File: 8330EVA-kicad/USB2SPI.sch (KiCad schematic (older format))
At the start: 8 parts

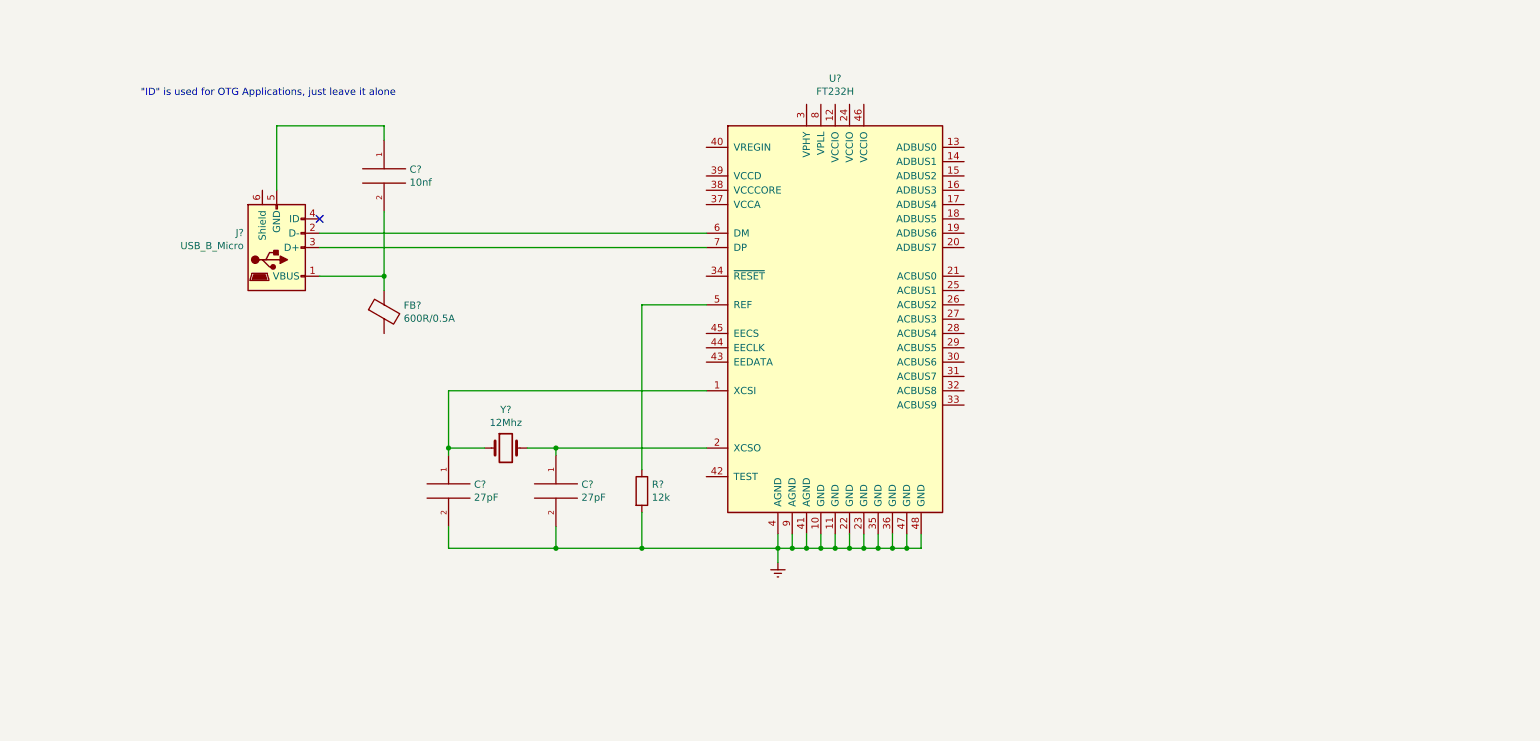
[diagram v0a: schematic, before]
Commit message: 完成FT232驱动电路原理图的绘制，并未相关的元件添加了封装
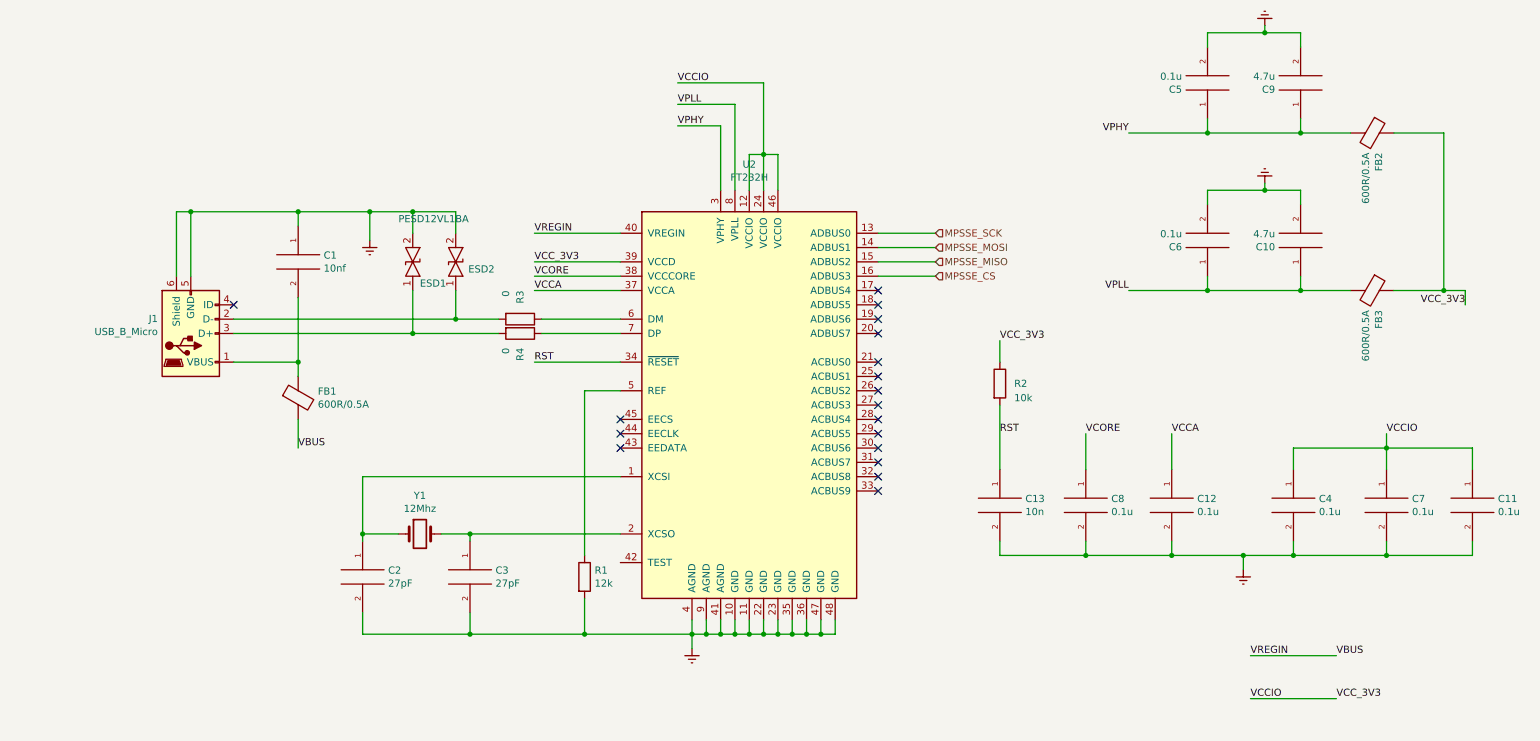
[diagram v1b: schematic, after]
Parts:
- added C10, C9: 4.7u, Capacitor_SMD:C_0603_1608Metric_Pad1.05x0.95mm_HandSolder, symbol pspice:CAP
- added C11, C12, C4, C5, C6, C7, C8: 0.1u, Capacitor_SMD:C_0603_1608Metric_Pad1.05x0.95mm_HandSolder, symbol pspice:CAP
- added C13: 10n, Capacitor_SMD:C_0603_1608Metric_Pad1.05x0.95mm_HandSolder, symbol pspice:CAP
- added ESD1, ESD2: PESD12VL1BA, Diode_SMD:D_SOD-323_HandSoldering, symbol 8330_EVA-extra:PESD12VL1BA
- added FB2, FB3: 600R/0.5A, Resistor_SMD:R_0805_2012Metric_Pad1.15x1.40mm_HandSolder, symbol Device:Ferrite_Bead
- added R2: 10k, Resistor_SMD:R_0805_2012Metric_Pad1.15x1.40mm_HandSolder, symbol Device:R
- added R3, R4: 0, Resistor_SMD:R_0805_2012Metric_Pad1.15x1.40mm_HandSolder, symbol Device:R
- C1, C2, C3: renamed from C?; footprint (none) -> Capacitor_SMD:C_0603_1608Metric_Pad1.05x0.95mm_HandSolder
- FB1: renamed from FB?; footprint (none) -> Resistor_SMD:R_0805_2012Metric_Pad1.15x1.40mm_HandSolder
- J1: renamed from J?; footprint (none) -> Connector_USB:USB_Micro-B_Wuerth_614105150721_Vertical
- R1: renamed from R?; footprint (none) -> Resistor_SMD:R_0805_2012Metric_Pad1.15x1.40mm_HandSolder
- U2: renamed from U?; footprint (none) -> Package_QFP:LQFP-48_7x7mm_P0.5mm
- Y1: renamed from Y?; footprint (none) -> Crystal:Crystal_SMD_5032-2Pin_5.0x3.2mm_HandSoldering
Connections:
- net Earth: now also C1.1, J1.5 (GND), J1.6 (Shield), C10.2, C11.2, C12.2, C13.2, C4.2, C5.2, C6.2, C7.2, C8.2, C9.2, ESD1.2, ESD2.2
- net VCCIO: now reaches U2.12 (VCCIO)
- net VCCIO: now also U2.24 (VCCIO), U2.39 (VCCD), U2.46 (VCCIO), C11.1, C4.1, C7.1, FB2.1, FB3.1, R2.1
- net MPSSE_SCK: now reaches U2.13 (ADBUS0)
- net MPSSE_MOSI: now reaches U2.14 (ADBUS1)
- net MPSSE_MISO: now reaches U2.15 (ADBUS2)
- net MPSSE_CS: now reaches U2.16 (ADBUS3)
- net VPHY: now reaches U2.3 (VPHY)
- net VPHY: now also C5.1, C9.1, FB2.2
- net RST: now reaches U2.34 (~RESET)
- net RST: now also C13.1, R2.2
- net VCCA: now reaches U2.37 (VCCA)
- net VCCA: now also C12.1
- net VCORE: now reaches U2.38 (VCCCORE)
- net VCORE: now also C8.1
- net VBUS: now reaches U2.40 (VREGIN)
- net VBUS: now also FB1.2
- net at U2.6 (DM): now also R3.1; no longer J1.2 (D-)
- net at U2.7 (DP): now also R4.1; no longer J1.3 (D+)
- net VPLL: now reaches U2.8 (VPLL)
- net VPLL: now also C10.1, C6.1, FB3.2
- new net: ESD2.1, J1.2 (D-), R3.2
- new net: ESD1.1, J1.3 (D+), R4.2
- no-connect marks 1 -> 18
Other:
- note removed: ""ID" is used for OTG Applications, just leave it alone\n"
- moved on the sheet: C1, C2, C3, FB1, J1, R1, U2, Y1

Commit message: 添加DAC部分/修改FT232供电方式（原理图）
1. 完成AD5312及REF192组成的程控信号产生部分原理图绘制
2. 修改FT232H的供电方式，添加了3.3VLDO，从之前的BUS-Power改为Self_Power
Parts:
- removed J1: USB_B_Micro, Connector_USB:USB_Micro-B_Wuerth_614105150721_Vertical, symbol Connector:USB_B_Micro
- added C?: 4.7u, symbol Device:C
- added C? (x2): 100n, symbol Device:C
- added U?: AMS1117-3.3, Package_TO_SOT_SMD:SOT-223-3_TabPin2, symbol Regulator_Linear:AMS1117-3.3
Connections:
- net VBUS: no longer U2.40 (VREGIN)
- net VCCIO: now also U2.40 (VREGIN), C?.1, U?.2 (VO)
- net USB_D-: now reaches ESD2.1, R3.2
- net USB_D+: now reaches ESD1.1, R4.2
- net Earth renamed Ground
- net Ground: now also C?.2, C?.2, C?.2, U?.1 (GND)
- new net VCC_+5V: C?.1, C?.1, U?.3 (VI)
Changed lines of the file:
@@
 	6200 5850 6100 5850
 Connection ~ 6100 5850
-$Comp
-L power:Earth #PWR0101
-U 1 1 5BEE6A05
-P 5200 5950
-F 0 "#PWR0101" H 5200 5700 50  0001 C CNN
-F 1 "Earth" H 5200 5800 50  0001 C CNN
-F 2 "" H 5200 5950 50  0001 C CNN
-F 3 "~" H 5200 5950 50  0001 C CNN
-	1    5200 5950
-	1    0    0    -1
-$EndComp
-Wire Wire Line
-	5200 5950 5200 5850
 Connection ~ 5200 5850
 $Comp
@@
 $EndComp
 $Comp
-L Connector:USB_B_Micro J1
-U 1 1 5BEF4049
-P 1700 3750
-F 0 "J1" H 1470 3647 50  0000 R CNN
-F 1 "USB_B_Micro" H 1470 3738 50  0000 R CNN
-F 2 "Connector_USB:USB_Micro-B_Wuerth_614105150721_Vertical" H 1850 3700 50  0001 C CNN
-F 3 "~" H 1850 3700 50  0001 C CNN
-	1    1700 3750
-	1    0    0    1
-$EndComp
-$Comp
 L Device:Ferrite_Bead FB1
 U 1 1 5BEFC068
@@
 	1    0    0    -1
 $EndComp
-Wire Wire Line
-	2450 4050 2450 3950
-Wire Wire Line
-	2450 3950 2000 3950
 $Comp
 L pspice:CAP C1
@@
 $EndComp
 Wire Wire Line
-	2450 3500 2450 3950
-Connection ~ 2450 3950
-Wire Wire Line
 	2450 3000 2450 2900
-Wire Wire Line
-	2450 2900 1700 2900
 NoConn ~ 2000 3550
-Text Label 2450 4550 0    50   ~ 0
-VBUS
-Wire Wire Line
-	2450 4550 2450 4350
 $Comp
 L pspice:CAP C6
@@
 	9450 2850 9450 2750
 Wire Wire Line
-	9450 2750 9200 2750
-Wire Wire Line
 	8800 2750 8800 2850
-$Comp
-L power:Earth #PWR0102
-U 1 1 5BEF366D
-P 9200 2700
-F 0 "#PWR0102" H 9200 2450 50  0001 C CNN
-F 1 "Earth" H 9200 2550 50  0001 C CNN
-F 2 "" H 9200 2700 50  0001 C CNN
-F 3 "~" H 9200 2700 50  0001 C CNN
-	1    9200 2700
-	-1   0    0    1
-$EndComp
-Wire Wire Line
-	9200 2700 9200 2750
-Connection ~ 9200 2750
-Wire Wire Line
-	9200 2750 8800 2750
 Text Label 10600 3550 2    50   ~ 0
 VCC_3V3
@@
 	9450 1750 9450 1650
 Wire Wire Line
-	9450 1650 9200 1650
-Wire Wire Line
 	8800 1650 8800 1750
-$Comp
-L power:Earth #PWR0103
-U 1 1 5BF0C20C
-P 9200 1600
-F 0 "#PWR0103" H 9200 1350 50  0001 C CNN
-F 1 "Earth" H 9200 1450 50  0001 C CNN
-F 2 "" H 9200 1600 50  0001 C CNN
-F 3 "~" H 9200 1600 50  0001 C CNN
-	1    9200 1600
-	-1   0    0    1
-$EndComp
-Wire Wire Line
-	9200 1600 9200 1650
-Connection ~ 9200 1650
-Wire Wire Line
-	9200 1650 8800 1650
 Wire Wire Line
 	9450 3450 8800 3450
@@
 F 3 "~" H 8550 4950 50  0001 C CNN
 	1    8550 4950
-	1    0    0    -1
-$EndComp
-$Comp
-L power:Earth #PWR0106
-U 1 1 5BF7B162
-P 9050 5400
-F 0 "#PWR0106" H 9050 5150 50  0001 C CNN
-F 1 "Earth" H 9050 5250 50  0001 C CNN
-F 2 "" H 9050 5400 50  0001 C CNN
-F 3 "~" H 9050 5400 50  0001 C CNN
-	1    9050 5400
 	1    0    0    -1
 $EndComp
@@
 	3250 2900 3550 2900
 Wire Wire Line
-	1700 2900 1700 3350
-Wire Wire Line
-	1600 2900 1700 2900
-Connection ~ 1700 2900
-Wire Wire Line
 	3650 5850 4450 5850
 $Comp
@@
 Connection ~ 3250 3750
 Wire Wire Line
-	3250 3750 2000 3750
-Wire Wire Line
 	3250 3750 3850 3750
 Wire Wire Line
 	3250 3450 3250 3750
-Wire Wire Line
-	2000 3650 3550 3650
 Connection ~ 3550 3650
-Wire Wire Line
-	2450 2900 2950 2900
 Connection ~ 2450 2900
 Connection ~ 3250 2900
-$Comp
-L power:Earth #PWR0107
-U 1 1 5C04C01A
-P 2950 3100
-F 0 "#PWR0107" H 2950 2850 50  0001 C CNN
-F 1 "Earth" H 2950 2950 50  0001 C CNN
-F 2 "" H 2950 3100 50  0001 C CNN
-F 3 "~" H 2950 3100 50  0001 C CNN
-	1    2950 3100
-	1    0    0    -1
-$EndComp
-Wire Wire Line
-	2950 3100 2950 2900
-Connection ~ 2950 2900
-Wire Wire Line
-	2950 2900 3250 2900
 Wire Wire Line
 	4100 3050 4700 3050
 Text Label 4100 3050 0    50   ~ 0
 VREGIN
-Text Label 9100 6300 0    50   ~ 0
+Text Label 2250 6500 0    50   ~ 0
 VCCIO
-Text Label 9700 6300 0    50   ~ 0
+Text Label 2850 6500 0    50   ~ 0
 VCC_3V3
 Wire Wire Line
-	9700 6300 9100 6300
+	2850 6500 2550 6500
 Wire Wire Line
 	7950 4450 7950 4700
@@
 Wire Wire Line
 	9400 5200 9400 5300
-Wire Wire Line
-	9400 5300 9050 5300
 Connection ~ 8550 5300
 Wire Wire Line
@@
 	10650 5300 10050 5300
 Connection ~ 10050 5300
-Wire Wire Line
-	9050 5400 9050 5300
-Connection ~ 9050 5300
-Wire Wire Line
-	9050 5300 8550 5300
-Text Label 9100 6000 0    50   ~ 0
+Text Label 2550 6200 0    50   ~ 0
 VREGIN
-Text Label 9700 6000 0    50   ~ 0
-VBUS
-Wire Wire Line
-	9100 6000 9700 6000
 Text Label 4100 3250 0    50   ~ 0
 VCC_3V3
 Wire Wire Line
 	4100 3250 4700 3250
-Wire Wire Line
-	1600 2900 1600 3350
 $Comp
 L Device:R R2
@@
 Wire Wire Line
 	4100 3950 4700 3950
+Text HLabel 950  3750 0    50   Input ~ 0
+USB_D+
+Text HLabel 950  3650 0    50   Input ~ 0
+USB_D-
+Text HLabel 900  4700 0    50   Input ~ 0
+VBUS
+Text HLabel 950  2900 0    50   Input ~ 0
+Ground
+Wire Wire Line
+	900  4700 2450 4700
+Wire Wire Line
+	2450 4350 2450 4700
+Wire Wire Line
+	950  3750 3250 3750
+Wire Wire Line
+	950  3650 3550 3650
+Wire Wire Line
+	950  2900 1400 2900
+Wire Wire Line
+	2450 3500 2450 4050
+Wire Wire Line
+	2450 2900 3250 2900
+Wire Wire Line
+	1400 2900 1400 5850
+Connection ~ 1400 2900
+Wire Wire Line
+	1400 2900 2450 2900
+Connection ~ 2900 5850
+Wire Wire Line
+	7350 5300 7350 5850
+Wire Wire Line
+	7350 5850 6200 5850
+Connection ~ 7350 5300
+Connection ~ 6200 5850
+Wire Wire Line
+	8550 5300 9100 5300
+Wire Wire Line
+	8800 1650 9100 1650
+Wire Wire Line
+	9100 1650 9100 2750
+Connection ~ 9100 1650
+Wire Wire Line
+	9100 1650 9450 1650
+Connection ~ 9100 2750
+Wire Wire Line
+	9100 2750 8800 2750
+Wire Wire Line
+	9100 2750 9450 2750
+Wire Wire Line
+	9100 2750 9100 5300
+Connection ~ 9100 5300
+Wire Wire Line
+	9100 5300 9400 5300
+$Comp
+L Regulator_Linear:AMS1117-3.3 U?
+U 1 1 5C1170A7
+P 2100 5150
+F 0 "U?" H 2100 5392 50  0000 C CNN
+F 1 "AMS1117-3.3" H 2100 5301 50  0000 C CNN
+F 2 "Package_TO_SOT_SMD:SOT-223-3_TabPin2" H 2100 5350 50  0001 C CNN
+F 3 "http://www.advanced-monolithic.com/pdf/ds1117.pdf" H 2200 4900 50  0001 C CNN
+	1    2100 5150
+	1    0    0    -1
+$EndComp
+Text HLabel 900  5150 0    50   Input ~ 0
+VCC_+5V
+$Comp
+L Device:C C?
+U 1 1 5C11D7BE
+P 1100 5500
+F 0 "C?" H 1215 5546 50  0000 L CNN
+F 1 "4.7u" H 1215 5455 50  0000 L CNN
+F 2 "" H 1138 5350 50  0001 C CNN
+F 3 "~" H 1100 5500 50  0001 C CNN
+	1    1100 5500
+	1    0    0    -1
+$EndComp
+$Comp
+L Device:C C?
+U 1 1 5C11DF65
+P 1650 5500
+F 0 "C?" H 1765 5546 50  0000 L CNN
+F 1 "100n" H 1765 5455 50  0000 L CNN
+F 2 "" H 1688 5350 50  0001 C CNN
+F 3 "~" H 1650 5500 50  0001 C CNN
+	1    1650 5500
+	1    0    0    -1
+$EndComp
+Wire Wire Line
+	1650 5350 1650 5150
+Wire Wire Line
+	900  5150 1100 5150
+Connection ~ 1650 5150
+Wire Wire Line
+	1650 5150 1800 5150
+Wire Wire Line
+	1100 5350 1100 5150
+Connection ~ 1100 5150
+Wire Wire Line
+	1100 5150 1650 5150
+Wire Wire Line
+	1100 5650 1100 5850
+Wire Wire Line
+	1100 5850 1400 5850
+Connection ~ 1400 5850
+Wire Wire Line
+	1400 5850 1650 5850
+Wire Wire Line
+	1650 5650 1650 5850
+Connection ~ 1650 5850
+Wire Wire Line
+	2100 5450 2100 5850
+Wire Wire Line
+	1650 5850 2100 5850
+Connection ~ 2100 5850
+$Comp
+L Device:C C?
+U 1 1 5C137049
+P 2500 5500
+F 0 "C?" H 2615 5546 50  0000 L CNN
+F 1 "100n" H 2550 5400 50  0000 L CNN
+F 2 "" H 2538 5350 50  0001 C CNN
+F 3 "~" H 2500 5500 50  0001 C CNN
+	1    2500 5500
+	1    0    0    -1
+$EndComp
+Wire Wire Line
+	2500 5150 2400 5150
+Wire Wire Line
+	2100 5850 2500 5850
+Wire Wire Line
+	2500 5650 2500 5850
+Connection ~ 2500 5850
+Wire Wire Line
+	2500 5850 2900 5850
+Text Label 2500 4850 0    50   ~ 0
+VREGIN
+Wire Wire Line
+	2500 4850 2500 5150
+Connection ~ 2500 5150
+Wire Wire Line
+	2500 5150 2500 5350
+Wire Wire Line
+	2550 6200 2550 6500
+Connection ~ 2550 6500
+Wire Wire Line
+	2550 6500 2250 6500
 $EndSCHEMATC

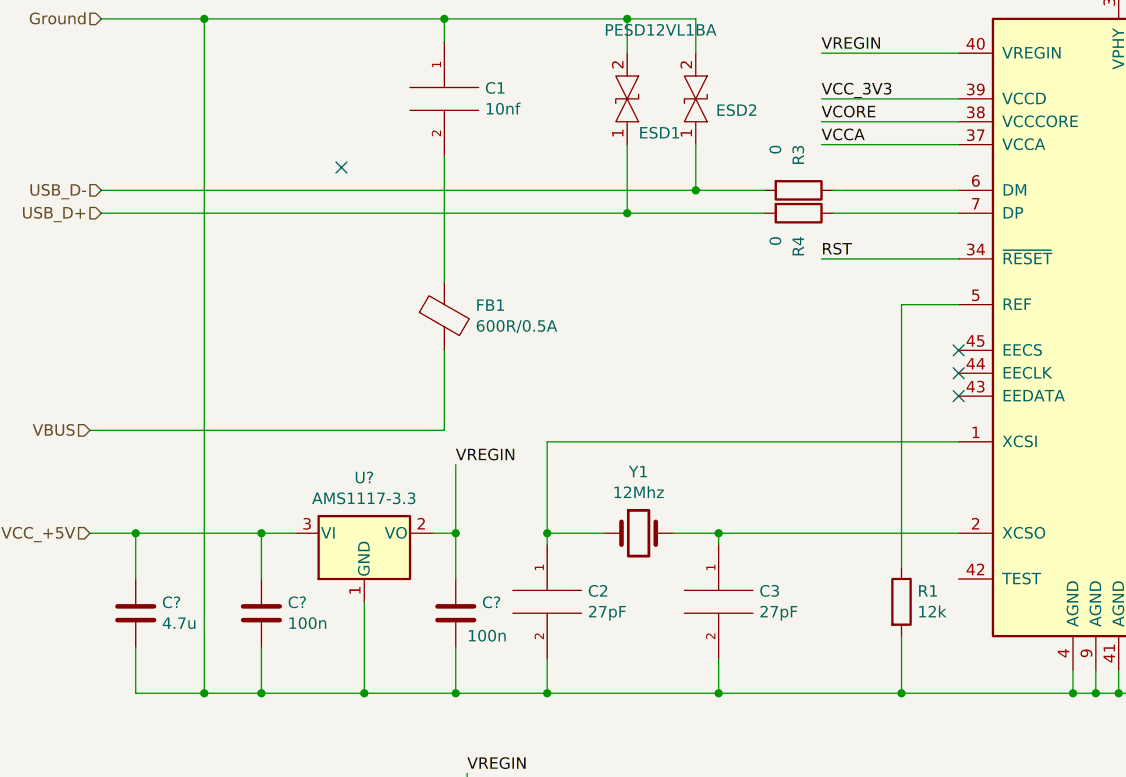
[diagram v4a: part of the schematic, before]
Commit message: 修复若干ERC未连接错误
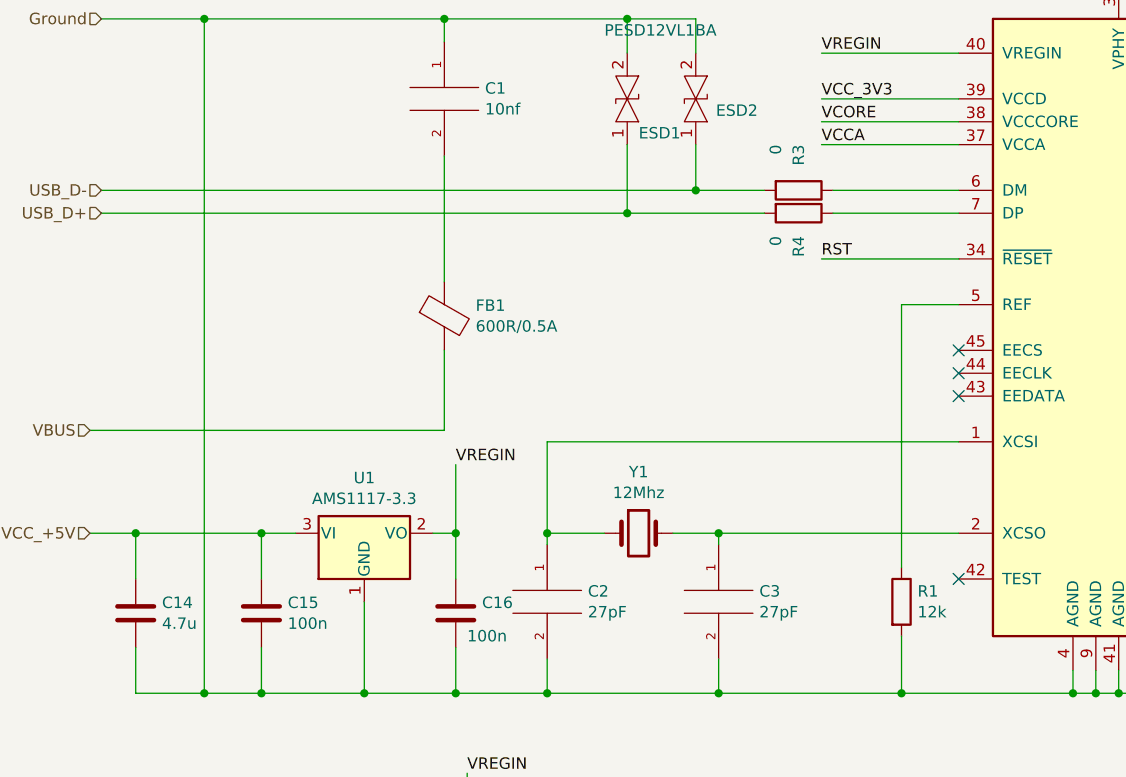
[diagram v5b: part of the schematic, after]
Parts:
- gave numbers to parts that had none: 4
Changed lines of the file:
@@
 Wire Wire Line
 	2450 3000 2450 2900
-NoConn ~ 2000 3550
 $Comp
 L pspice:CAP C6
@@
 	9100 5300 9400 5300
 $Comp
-L Regulator_Linear:AMS1117-3.3 U?
+L Regulator_Linear:AMS1117-3.3 U1
 U 1 1 5C1170A7
 P 2100 5150
-F 0 "U?" H 2100 5392 50  0000 C CNN
+F 0 "U1" H 2100 5392 50  0000 C CNN
 F 1 "AMS1117-3.3" H 2100 5301 50  0000 C CNN
 F 2 "Package_TO_SOT_SMD:SOT-223-3_TabPin2" H 2100 5350 50  0001 C CNN
@@
 VCC_+5V
 $Comp
-L Device:C C?
+L Device:C C14
 U 1 1 5C11D7BE
 P 1100 5500
-F 0 "C?" H 1215 5546 50  0000 L CNN
+F 0 "C14" H 1215 5546 50  0000 L CNN
 F 1 "4.7u" H 1215 5455 50  0000 L CNN
 F 2 "" H 1138 5350 50  0001 C CNN
@@
 $EndComp
 $Comp
-L Device:C C?
+L Device:C C15
 U 1 1 5C11DF65
 P 1650 5500
-F 0 "C?" H 1765 5546 50  0000 L CNN
+F 0 "C15" H 1765 5546 50  0000 L CNN
 F 1 "100n" H 1765 5455 50  0000 L CNN
 F 2 "" H 1688 5350 50  0001 C CNN
@@
 Connection ~ 2100 5850
 $Comp
-L Device:C C?
+L Device:C C16
 U 1 1 5C137049
 P 2500 5500
-F 0 "C?" H 2615 5546 50  0000 L CNN
+F 0 "C16" H 2615 5546 50  0000 L CNN
 F 1 "100n" H 2550 5400 50  0000 L CNN
 F 2 "" H 2538 5350 50  0001 C CNN
@@
 Wire Wire Line
 	2550 6500 2250 6500
+NoConn ~ 4700 5350
 $EndSCHEMATC

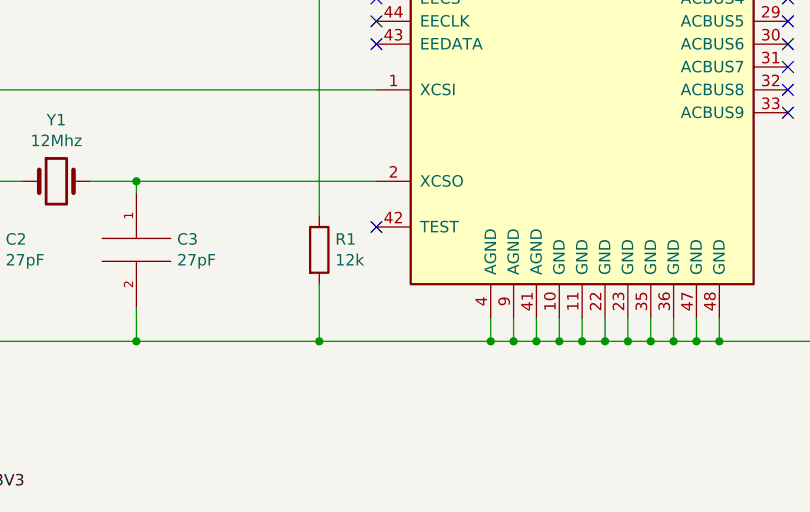
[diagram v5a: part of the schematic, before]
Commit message: 修复FT232 Test脚链接错误
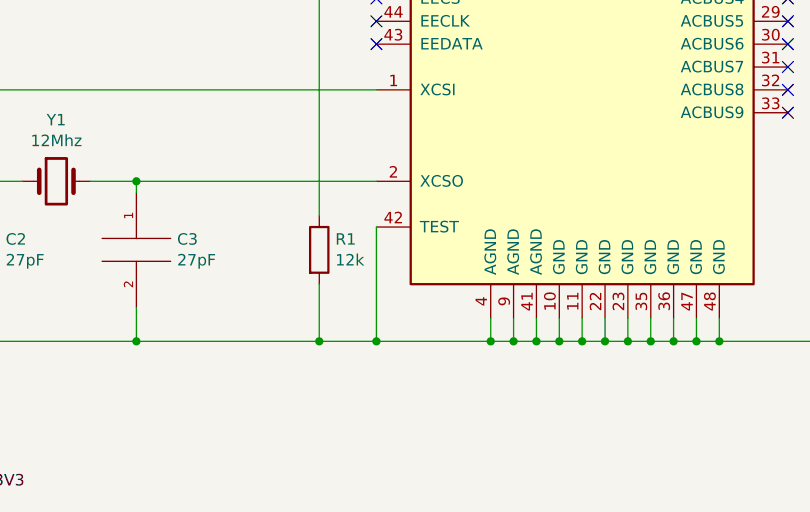
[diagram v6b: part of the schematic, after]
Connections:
- net Ground: now also U2.42 (TEST)
- no-connect marks 18 -> 17
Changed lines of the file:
@@
 Connection ~ 4450 5850
 Wire Wire Line
-	4450 5850 5200 5850
+	4450 5850 4700 5850
 NoConn ~ 4700 4350
 NoConn ~ 4700 4450
@@
 Wire Wire Line
 	2550 6500 2250 6500
-NoConn ~ 4700 5350
+Wire Wire Line
+	4700 5350 4700 5850
+Connection ~ 4700 5850
+Wire Wire Line
+	4700 5850 5200 5850
 $EndSCHEMATC
